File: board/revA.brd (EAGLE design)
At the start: 50 x 50 mm, 47 parts, among them IC1 74HCT125, Q1 VND7NV04, Q2 VND7NV04, Q3 VND7NV04, Q4 VND7NV04

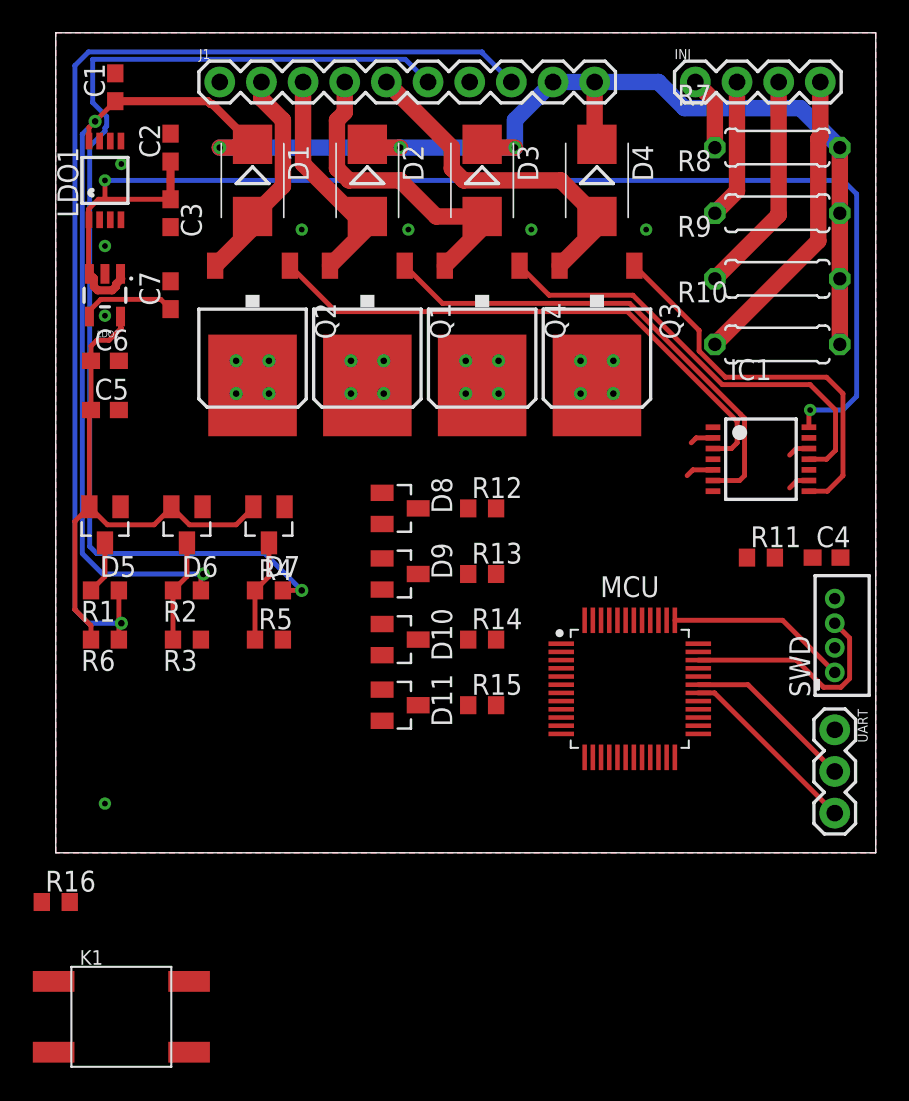
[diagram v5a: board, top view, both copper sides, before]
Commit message: More routing, adding interfaces
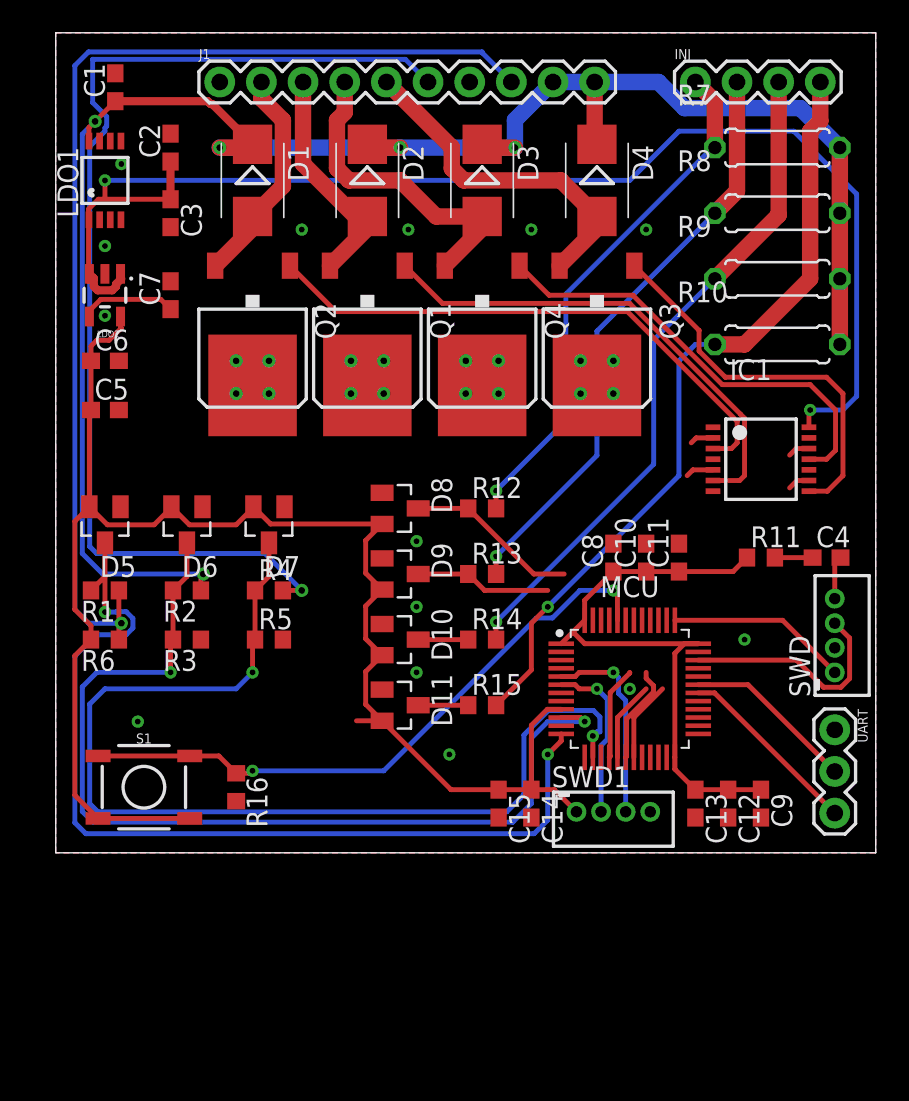
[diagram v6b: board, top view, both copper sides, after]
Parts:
- removed K1: (no value), Seeed-Switch:SW4-SMD-6.0X6.0X5.0MM
- added C10, C11, C12, C13, C15: 100nF 5v, rcl:C0603
- added C14, C8, C9: 4.7uF 5v, rcl:C0603
- added S1: (no value), SparkFun-Switches:TACTILE_SWITCH_SMD_5.2MM
- added SWD1: B4B-ZR, con-jst:B4B-ZR
- moved R16 13.0 mm to (11.0, 4.00), turned to 270 degrees
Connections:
- removed net N$3: K1.1, K1.4, MCU.44, R16.1
- new net I2C_SCL: MCU.6, SWD1.2
- new net I2C_SDA: MCU.5, SWD1.3
- new net N$5: MCU.44, R16.1, S1.1, S1.2
- net +3V3: now also C10.1, C11.1, C12.1, C13.1, C14.1, C15.1, C8.1, C9.1, S1.3, S1.4, SWD1.1; no longer K1.2, K1.3
- net FF_FREQ: now also MCU.12
- net GND: now also C10.2, C11.2, C12.2, C13.2, C14.2, C15.2, C8.2, C9.2, SWD1.4
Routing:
- net +3V3: track 33.6 -> 132.4 mm
- net AN_1: track 6.25 -> 64.0 mm, vias 0 -> 2
- net FF_FREQ: track 3.25 -> 57.7 mm, vias 0 -> 2
- net AN_0: track 6.25 -> 59.0 mm, vias 0 -> 2
- net N$5: track 0.00 -> 38.4 mm, vias 0 -> 2
- net INJ4_IN: track 18.7 -> 47.9 mm, vias 0 -> 1
- net INJ1_IN: track 4.49 -> 32.1 mm, vias 0 -> 1
- net INJ3_IN: track 13.6 -> 41.1 mm, vias 0 -> 1
- net INJ2_IN: track 8.56 -> 36.1 mm, vias 0 -> 1
- net INJ1_FREQ: track 0.00 -> 16.3 mm
- net INJ2_FREQ: track 0.00 -> 13.2 mm
- net I2C_SDA: track 0.00 -> 12.1 mm, vias 0 -> 1
- net I2C_SCL: track 0.00 -> 10.2 mm, vias 0 -> 1
- net INJ3_FREQ: track 0.00 -> 9.12 mm
- net INJ4_FREQ: track 0.00 -> 7.95 mm
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
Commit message: Routing
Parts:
- moved R11 4.47 mm to (47.0, 20.0)
- moved C10 1.00 mm to (36.0, 19.0)
- moved C11 1.00 mm to (38.0, 19.0)
- moved C12 1.00 mm to (42.0, 3.00)
- moved C13 1.00 mm to (40.0, 3.00)
- moved C8 1.00 mm to (34.0, 19.0)
- moved C9 1.00 mm to (44.0, 3.00)
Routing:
- net INJ4_FREQ: track 7.95 -> 37.4 mm, vias 0 -> 2
- net +3V3: track 132.4 -> 157.1 mm, vias 0 -> 3
- net INJ3_TRIGGER: track 1.34 -> 22.8 mm
- net INJ2_TRIGGER: track 1.72 -> 18.1 mm, vias 0 -> 2
- net INJ3_FREQ: track 9.12 -> 24.8 mm, vias 0 -> 2
- net INJ4_TRIGGER: track 1.36 -> 16.8 mm
- net INJ1_TRIGGER: track 1.45 -> 16.8 mm, vias 0 -> 2
- net INJ2_FREQ: track 13.2 -> 23.4 mm
- net N$9: track 27.2 -> 23.3 mm
- net N$10: track 24.2 -> 23.0 mm, vias 0 -> 2
- net INJ1_FREQ: track 16.3 -> 17.3 mm
- net N$5: track 38.4 -> 37.4 mm, vias 2 -> 1

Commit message: Testing autorouter
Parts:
- removed SWD1: B4B-ZR, con-jst:B4B-ZR
- added I2C: B4B-ZR, con-jst:B4B-ZR
- moved C14 16.0 mm to (30.0, 19.0), turned to 90 degrees
- moved C15 16.0 mm to (28.0, 19.0), turned to 90 degrees
- moved D10 3.00 mm to (18.0, 13.0)
- moved D11 3.00 mm to (18.0, 9.00)
- moved D8 3.00 mm to (18.0, 21.0)
- moved D9 3.00 mm to (18.0, 17.0)
- moved R12 3.00 mm to (23.0, 21.0)
- moved R13 3.00 mm to (23.0, 17.0)
- moved R14 3.00 mm to (23.0, 13.0)
- moved R15 3.00 mm to (23.0, 9.00)
- moved C10 2.00 mm to (38.0, 19.0)
- moved C11 2.00 mm to (40.0, 19.0)
- moved C8 2.00 mm to (36.0, 19.0)
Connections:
- net +3V3: now also I2C.1; no longer SWD1.1
- net GND: now also I2C.4; no longer SWD1.4
- net I2C_SCL: now also I2C.2; no longer SWD1.2
- net I2C_SDA: now also I2C.3; no longer SWD1.3
- net INJ1: now also Q3.3; no longer Q2.3
- net INJ1_TRIGGER: now also IC1.9; no longer IC1.2
- net INJ2: now also Q4.3; no longer Q1.3
- net INJ2_TRIGGER: now also IC1.12; no longer IC1.5
- net INJ3: now also Q1.3; no longer Q4.3
- net INJ3_TRIGGER: now also IC1.5; no longer IC1.12
- net INJ4: now also Q2.3; no longer Q3.3
- net INJ4_TRIGGER: now also IC1.2; no longer IC1.9
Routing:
- net AN_1: track 64.3 -> 32.0 mm
- net NRST: track 2.64 -> 27.3 mm
- net INJ4: track 20.9 -> 45.6 mm, vias 0 -> 1
- net AN_0: track 59.0 -> 37.1 mm
- net FF_FREQ: track 57.7 -> 37.0 mm
- net INJ1_FREQ: track 17.3 -> 36.9 mm, vias 0 -> 3
- net INJ4_FREQ: track 37.4 -> 18.9 mm
- net AN1: track 66.7 -> 49.4 mm
- net INJ1: track 14.2 -> 30.4 mm
- net I2C_SCL: track 10.2 -> 25.5 mm
- net INJ3_TRIGGER: track 22.8 -> 12.1 mm, vias 0 -> 2
- net N$8: track 30.1 -> 40.0 mm, vias 0 -> 4
- net N$9: track 23.3 -> 31.4 mm, vias 0 -> 4
- net N$5: track 37.4 -> 45.0 mm, vias 1 -> 4
- net INJ3: track 19.5 -> 26.5 mm, vias 0 -> 1
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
